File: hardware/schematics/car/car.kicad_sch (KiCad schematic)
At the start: 21 parts, among them M1 Motor_Servo, Q1 PMOS, SW1 SW_SPST, SW2 SW_Push, SW3 SW_Push, U1 VL53L0CXV0DH1, U10 Mini-560, U11 JGA25-37x, U2 VL53L0CXV0DH1, U3 VL53L0CXV0DH1, U4 Pixy2, U6 TB6612FNG, U7 SparkFun OTOS, U8 SWD debug probe, U9 Mini-360

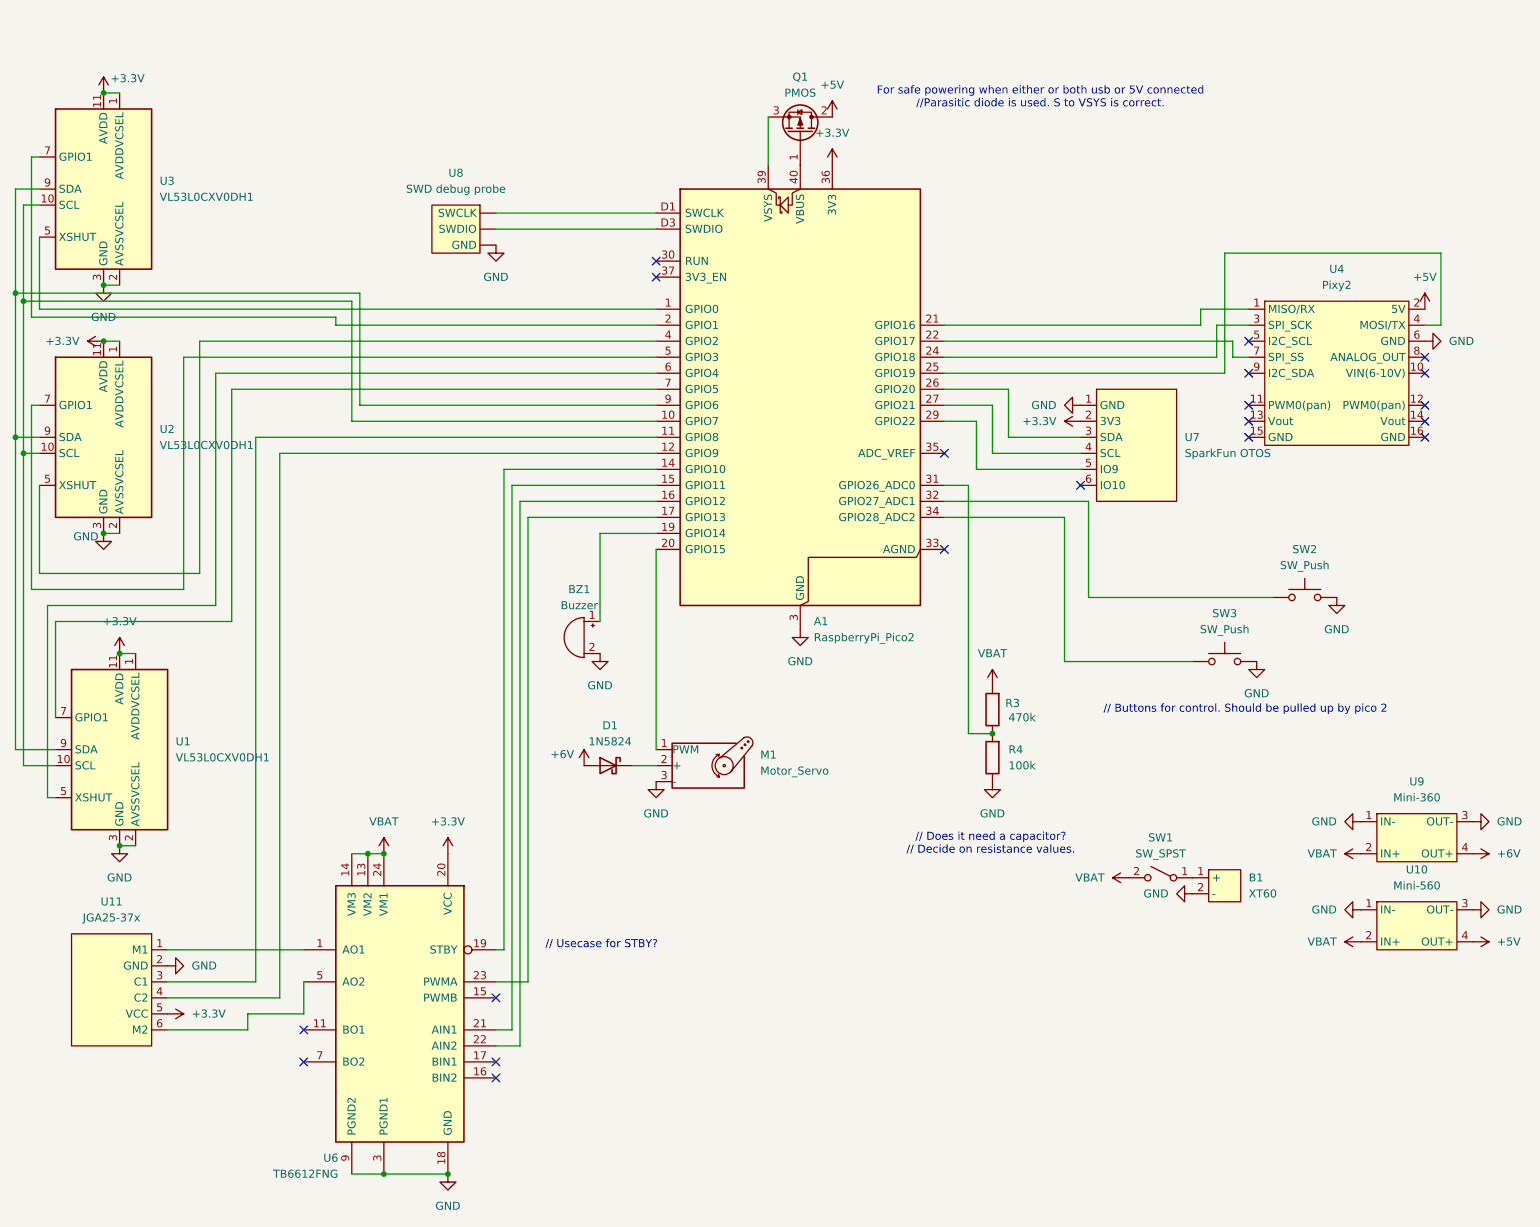
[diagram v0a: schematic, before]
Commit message: [Schematic] Alternative schematic.
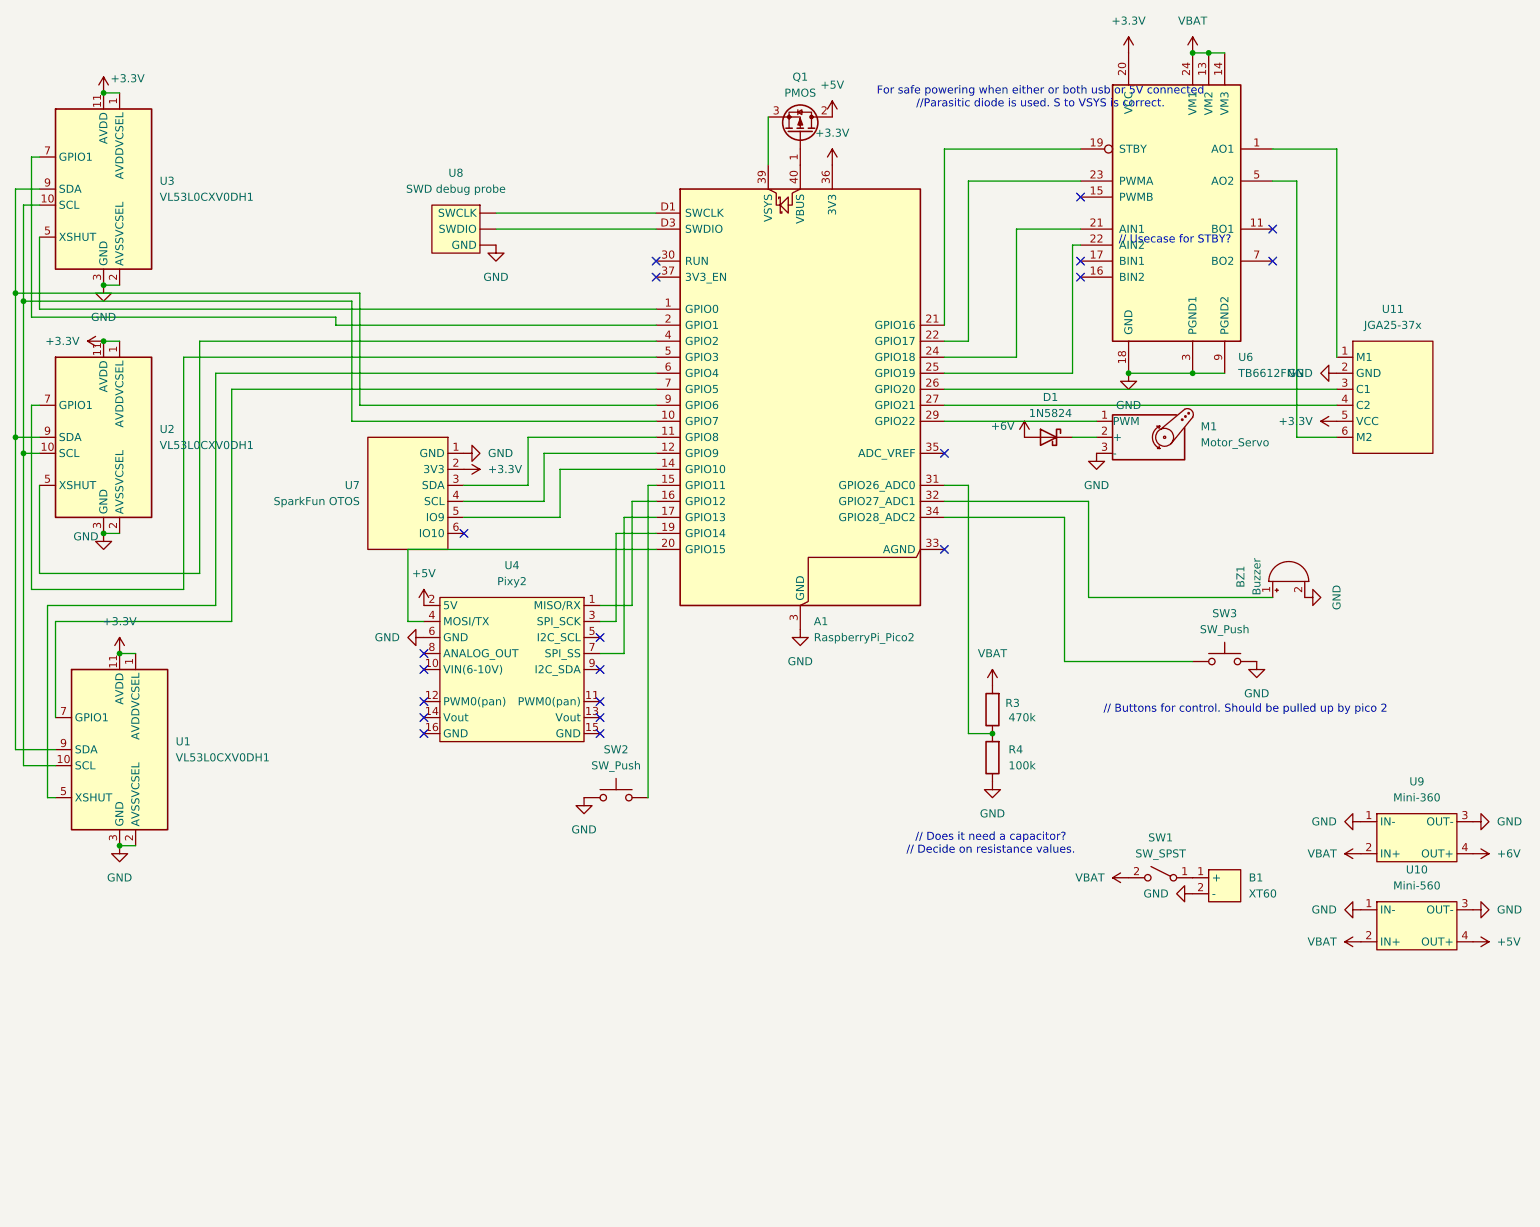
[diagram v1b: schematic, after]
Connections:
- net at U6.19 (STBY): now also A1.21 (GPIO16); no longer A1.14 (GPIO10)
- net at U6.21 (AIN1): now also A1.24 (GPIO18); no longer A1.15 (GPIO11)
- net at U6.22 (AIN2): now also A1.25 (GPIO19); no longer A1.16 (GPIO12)
- net at U6.23 (PWMA): now also A1.22 (GPIO17); no longer A1.17 (GPIO13)
- net at U11.3 (C1): now also A1.26 (GPIO20); no longer A1.11 (GPIO8)
- net at U11.4 (C2): now also A1.27 (GPIO21); no longer A1.12 (GPIO9)
- net at M1.1 (PWM): now also A1.29 (GPIO22); no longer A1.20 (GPIO15)
- net at BZ1.1 (+): now also A1.32 (GPIO27_ADC1); no longer A1.19 (GPIO14)
- net at U4.1 (MISO/RX): now also A1.16 (GPIO12); no longer A1.21 (GPIO16)
- net at U4.3 (SPI_SCK): now also A1.19 (GPIO14); no longer A1.24 (GPIO18)
- net at U4.4 (MOSI/TX): now also A1.20 (GPIO15); no longer A1.25 (GPIO19)
- net at U4.7 (SPI_SS): now also A1.17 (GPIO13); no longer A1.22 (GPIO17)
- net at U7.3 (SDA): now also A1.11 (GPIO8); no longer A1.26 (GPIO20)
- net at U7.4 (SCL): now also A1.12 (GPIO9); no longer A1.27 (GPIO21)
- net at U7.5 (IO9): now also A1.14 (GPIO10); no longer A1.29 (GPIO22)
- net at SW2.1: now also A1.15 (GPIO11); no longer A1.32 (GPIO27_ADC1)
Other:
- moved on the sheet: BZ1, D1, M1, SW2, U11, U4, U6

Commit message: [Schematic] PCB many things
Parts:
- U7: footprint Connector_PinHeader_2.54mm:PinHeader_1x05_P2.54mm_Vertical -> xlnc-foot:Sparkfun_OTOS_PinHeader_1x05_P2.54mm_Vertical
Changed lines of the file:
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@@
 			)
 		)
-		(property "Footprint" "Connector_PinHeader_2.54mm:PinHeader_1x05_P2.54mm_Vertical"
+		(property "Footprint" "xlnc-foot:Sparkfun_OTOS_PinHeader_1x05_P2.54mm_Vertical"
 			(at 85.09 81.28 0)
 			(hide yes)

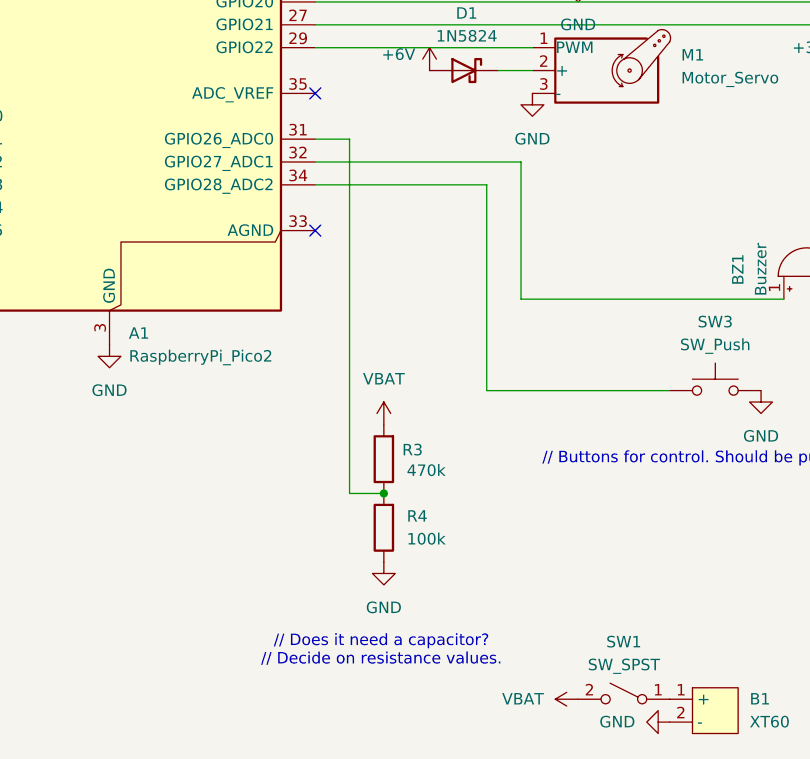
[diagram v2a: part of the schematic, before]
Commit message: [Schematic] Add ADC cap, place underneath pico it and buzzer.
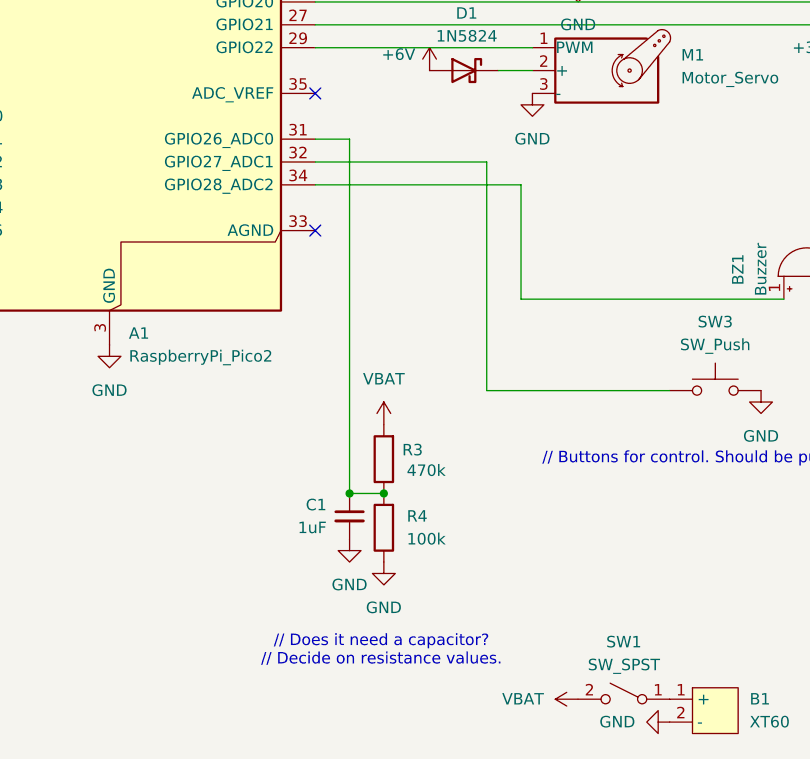
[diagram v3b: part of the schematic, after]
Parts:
- added C1: 1uF, Capacitor_THT:C_Axial_L5.1mm_D3.1mm_P7.50mm_Horizontal, symbol Device:C_Small
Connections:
- net GND: now also C1.2
- net at A1.31 (GPIO26_ADC0), R3.1, R4.2: now also C1.1
- net at BZ1.1 (+): now also A1.34 (GPIO28_ADC2); no longer A1.32 (GPIO27_ADC1)
- net at SW3.1: now also A1.32 (GPIO27_ADC1); no longer A1.34 (GPIO28_ADC2)
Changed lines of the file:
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@@
+	)
+	(junction
+		(at 167.64 119.38)
+		(diameter 0)
+		(color 0 0 0 0)
 	)
 	(junction
@@
 	(wire
 		(pts
-			(xy 182.88 107.95) (xy 182.88 85.09)
+			(xy 182.88 82.55) (xy 182.88 107.95)
 		)
 		(stroke
@@
 	(wire
 		(pts
+			(xy 186.69 85.09) (xy 163.83 85.09)
+		)
+		(stroke
+			(width 0)
+			(type default)
+		)
+	)
+	(wire
+		(pts
 			(xy 45.72 93.98) (xy 45.72 57.15)
 		)
@@
 	(wire
 		(pts
+			(xy 182.88 82.55) (xy 163.83 82.55)
+		)
+		(stroke
+			(width 0)
+			(type default)
+		)
+	)
+	(wire
+		(pts
 			(xy 17.78 124.46) (xy 22.86 124.46)
 		)
@@
 	(wire
 		(pts
+			(xy 186.69 97.79) (xy 186.69 85.09)
+		)
+		(stroke
+			(width 0)
+			(type default)
+		)
+	)
+	(wire
+		(pts
 			(xy 30.48 17.78) (xy 33.02 17.78)
 		)
@@
 	(wire
 		(pts
-			(xy 182.88 85.09) (xy 163.83 85.09)
-		)
-		(stroke
-			(width 0)
-			(type default)
-		)
-	)
-	(wire
-		(pts
 			(xy 203.2 11.43) (xy 205.74 11.43)
 		)
@@
 	(wire
 		(pts
-			(xy 186.69 82.55) (xy 163.83 82.55)
-		)
-		(stroke
-			(width 0)
-			(type default)
-		)
-	)
-	(wire
-		(pts
 			(xy 33.02 137.16) (xy 35.56 137.16)
 		)
@@
 		(pts
 			(xy 87.63 85.09) (xy 102.87 85.09)
-		)
-		(stroke
-			(width 0)
-			(type default)
-		)
-	)
-	(wire
-		(pts
-			(xy 186.69 97.79) (xy 186.69 82.55)
 		)
 		(stroke
@@
 	)
 	(symbol
+		(lib_id "power:GND")
+		(at 167.64 124.46 0)
+		(unit 1)
+		(body_style 1)
+		(exclude_from_sim no)
+		(in_bom yes)
+		(on_board yes)
+		(in_pos_files yes)
+		(dnp no)
+		(fields_autoplaced yes)
+		(property "Reference" "#PWR012"
+			(at 167.64 130.81 0)
+			(hide yes)
+			(show_name no)
+			(do_not_autoplace no)
+			(effects
+				(font
+					(size 1.27 1.27)
+				)
+			)
+		)
+		(property "Value" "GND"
+			(at 167.64 129.54 0)
+			(show_name no)
+			(do_not_autoplace no)
+			(effects
+				(font
+					(size 1.27 1.27)
+				)
+			)
+		)
+		(property "Footprint" ""
+			(at 167.64 124.46 0)
+			(hide yes)
+			(show_name no)
+			(do_not_autoplace no)
+			(effects
+				(font
+					(size 1.27 1.27)
+				)
+			)
+		)
+		(property "Datasheet" ""
+			(at 167.64 124.46 0)
+			(hide yes)
+			(show_name no)
+			(do_not_autoplace no)
+			(effects
+				(font
+					(size 1.27 1.27)
+				)
+			)
+		)
+		(property "Description" "Power symbol creates a global label with name \"GND\" , ground"
+			(at 167.64 124.46 0)
+			(hide yes)
+			(show_name no)
+			(do_not_autoplace no)
+			(effects
+				(font
+					(size 1.27 1.27)
+				)
+			)
+		)
+		(pin "1"
+		)
+		(instances
+			(project "car"
+				(path "/5e1ba60a-5dff-4ce7-a8b0-cf19f27fe16e"
+					(reference "#PWR012")
+					(unit 1)
+				)
+			)
+		)
+	)
+	(symbol
 		(lib_id "power:+3.3V")
 		(at 226.06 69.85 90)
@@
 					(unit 1)
 				)
+			)
+		)
+	)
+	(symbol
+		(lib_id "Device:C_Small")
+		(at 167.64 121.92 0)
+		(mirror y)
+		(unit 1)
+		(body_style 1)
+		(exclude_from_sim no)
+		(in_bom yes)
+		(on_board yes)
+		(in_pos_files yes)
+		(dnp no)
+		(property "Reference" "C1"
+			(at 165.1 120.6562 0)
+			(show_name no)
+			(do_not_autoplace no)
+			(effects
+				(font
+					(size 1.27 1.27)
+				)
+				(justify left)
+			)
+		)
+		(property "Value" "1uF"
+			(at 165.1 123.1962 0)
+			(show_name no)
+			(do_not_autoplace no)
+			(effects
+				(font
+					(size 1.27 1.27)
+				)
+				(justify left)
+			)
+		)
+		(property "Footprint" "Capacitor_THT:C_Axial_L5.1mm_D3.1mm_P7.50mm_Horizontal"
+			(at 167.64 121.92 0)
+			(hide yes)
+			(show_name no)
+			(do_not_autoplace no)
+			(effects
+				(font
+					(size 1.27 1.27)
+				)
+			)
+		)
+		(property "Datasheet" ""
+			(at 167.64 121.92 0)
+			(hide yes)
+			(show_name no)
+			(do_not_autoplace no)
+			(effects
+				(font
+					(size 1.27 1.27)
+				)
+			)
+		)
+		(property "Description" "Unpolarized capacitor, small symbol"
+			(at 167.64 121.92 0)
+			(hide yes)
+			(show_name no)
+			(do_not_autoplace no)
+			(effects
+				(font
+					(size 1.27 1.27)
+				)
+			)
+		)
+		(pin "1"
+		)
+		(pin "2"
+		)
+		(instances
+			(project "car"
+				(path "/5e1ba60a-5dff-4ce7-a8b0-cf19f27fe16e"
+					(reference "C1")
+					(unit 1)
+				)
